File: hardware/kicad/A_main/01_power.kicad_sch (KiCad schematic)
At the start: 24 parts, among them J1 XT60, Q1 DMP3098L, U1 TPS62130, U2 TPS62130, U3 TPS7A2033, U4 ADP150, U5 ADP150, U6 ADP150, U7 ADP150, U8 ADP150, U9 ADP150

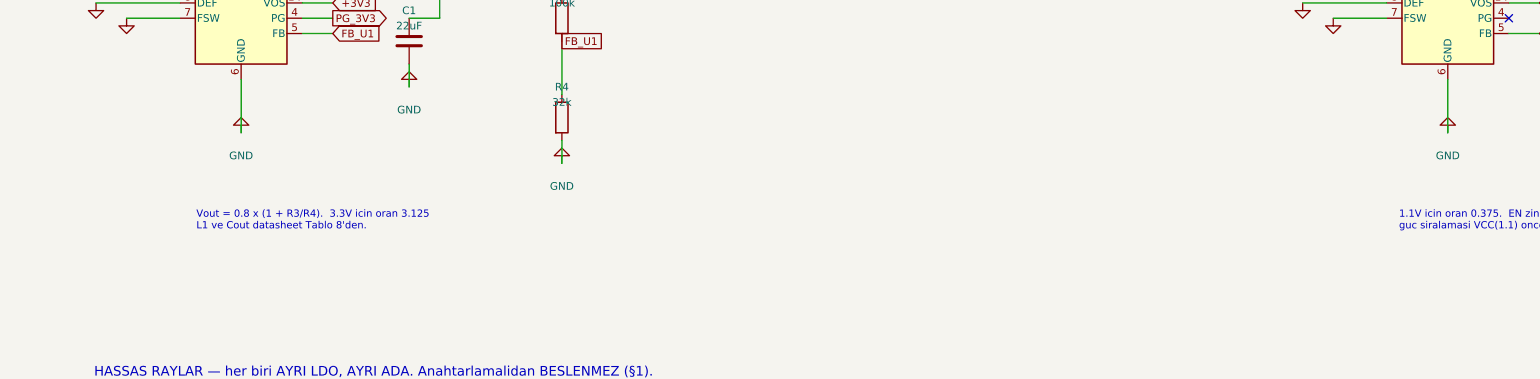
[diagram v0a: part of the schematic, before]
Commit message: Connect the pads that had no net
A symbol pin number must agree with the footprint pad number. If the
numbers do not agree, the net goes nowhere. The netlist removes it
and gives no message. ERC examines the schematic and sees a wire. DRC
does not count an unconnected pad as a violation. All three boards
showed zero ERC violations while 31 pads had no net.

Two of these faults stopped a board.

The footprint of the Ethernet PHY was for a different part. The
project used QFN-48 6x6 mm with 0.4 mm pitch. The RTL8211F(I)-CG is
WQFN-40-EP 5x5 mm. You cannot solder the part to that pad pattern.

The 25 MHz crystal had a 2-pin symbol on a 4-pad footprint. On a 3225
crystal the terminals are the diagonal pads 1 and 3. Pads 2 and 4 are
the metal can. XO went to pad 2. There was no crystal between XI and
XO, and thus neither PHY could make a clock.

The paddle of the AD9251 was pin 0 in the symbol and pad 65 in the
footprint. The paddle of the PE4312 was Pad against pad 21. The gas
discharge tubes had one electrode unconnected, because
Device:GDT_2Pin uses pins 1 and 3 but the varistor footprint uses
pads 1 and 2. A local footprint with pads 1 and 3 corrects this.

ped_denetim.py finds these faults on the board. yap.sh runs it before
the DSN export. The chain stops if a pad has no net.

The DSN export also changed. It declared In1 and In4 as power layers
but did not export the copper on them. The router thus believed that
the two ground planes were empty. It routed the 289 pins of GND as
traces on the signal layers. The planes now go out as conduction
areas.
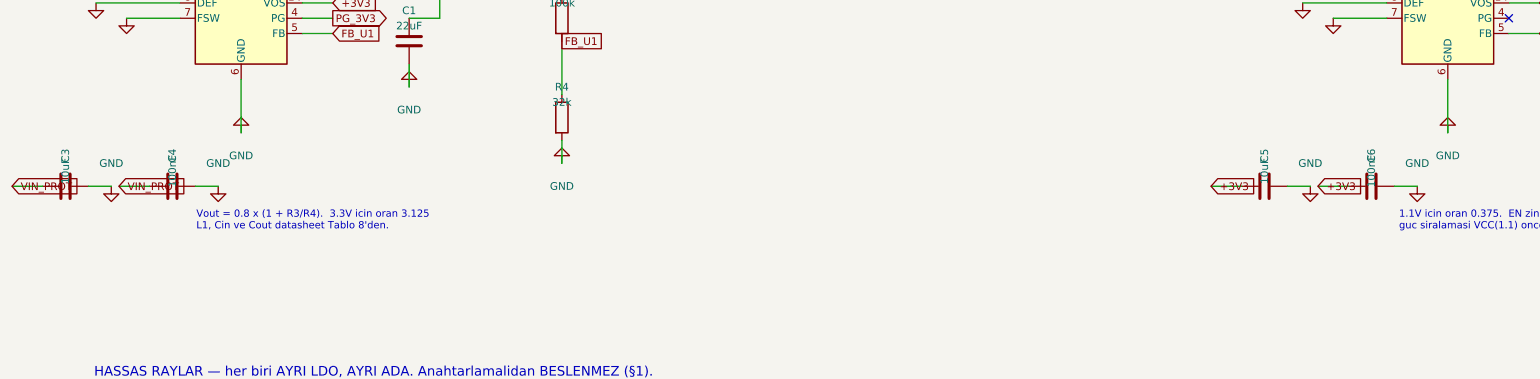
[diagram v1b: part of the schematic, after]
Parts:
- added C3: 10uF, Capacitor_SMD:C_1206_3216Metric, symbol Device:C
- added C4, C6: 100nF, Capacitor_SMD:C_0603_1608Metric, symbol Device:C
- added C5: 10uF, Capacitor_SMD:C_0805_2012Metric, symbol Device:C
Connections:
- net +3V3: now also C5.1, C6.1
- net GND: now also C3.2, C4.2, C5.2, C6.2
- net VIN_PROT: now also C3.1, C4.1
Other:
- note added: "Vout = 0.8 x (1 + R3/R4). 3.3V icin oran 3.125 L1, Cin ve Cout datasheet Tablo 8'den."
- note removed: "Vout = 0.8 x (1 + R3/R4). 3.3V icin oran 3.125 L1 ve Cout datasheet Tablo 8'den."

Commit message: Remove the pads that have no copper from the DSN export
The router reported the same 220 clearance violations in each pass.
At the same time the number of unrouted connections decreased. The
violations were thus in the input and not in the routing.

The -1EP footprints of KiCad put four paste apertures on the exposed
pad. These apertures stop full paste coverage and they have no copper
layer. The DSN export put them on the top copper layer. The image of
U51 in the DSN had 21 pins: 17 correct pins and four unconnected
copper islands in the exposed pad. These islands are always in
conflict with the pad and they close the area below it.

The export now removes a pad that has no copper layer. The image of
U51 has 17 pins. The violations on board D decreased from 220 to 152.
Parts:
- added C10, C11, C12, C13, C14, C15, C16, C17, C18, C19, C20, C21, C22, C23: 1uF, Capacitor_SMD:C_0603_1608Metric, symbol Device:C
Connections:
- net +1V8: now also C11.1
- net +1V8_A: now also C15.1
- net +1V8_CLK: now also C23.1
- net +1V8_D: now also C17.1
- net +2V5: now also C13.1, C22.1
- net +3V3: now also C10.1, C12.1, C14.1, C16.1, C18.1, C20.1
- net +3V3_A: now also C21.1
- net +3V3_CLK: now also C19.1
- net GND: now also C10.2, C11.2, C12.2, C13.2, C14.2, C15.2, C16.2, C17.2, C18.2, C19.2, C20.2, C21.2, C22.2, C23.2

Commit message: Give each regulator the part number its rail needs
A fixed-output LDO carries its voltage in the part number. If the
number is wrong the schematic does not change: the netlist is correct,
ERC is clean, DRC is clean, and the rail comes up at the wrong
voltage.

U3 was specified as TPS7A2033. The last two digits are the output, so
33 is 3.3 V and 18 is 1.8 V. Its output feeds +1V8, which supplies the
FPGA's bank 6 and 3 VCCIO across twenty pads. The wiring was correct
and only the part number was wrong.

The six ADP150 regulators all carried the value "ADP150" and collapsed
into one BOM line under one code, which is the 2.5 V version. Their
outputs are 1.8, 1.8, 1.8, 2.5, 3.3 and 3.3 V. That line would have
put 2.5 V on both ADC supplies, and the AD9251 has an absolute maximum
of 2.0 V on AVDD. Each rail now names its own variant and the BOM has
separate lines.

regulator_denetim checks this class. It reads the voltage from the
part number, reads it from the rail name and compares them. It also
requires an LDO to have an input higher than its output by at least
the dropout voltage.
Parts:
- U3: value TPS7A2033 -> TPS7A2018
- U4, U5, U9: value ADP150 -> ADP150-1.8
- U6, U7: value ADP150 -> ADP150-3.3
- U8: value ADP150 -> ADP150-2.5
